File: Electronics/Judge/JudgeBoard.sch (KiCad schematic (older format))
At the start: 21 parts, among them J1 RJ12-UNSHLD, U1 74HC165, U2 74HC165

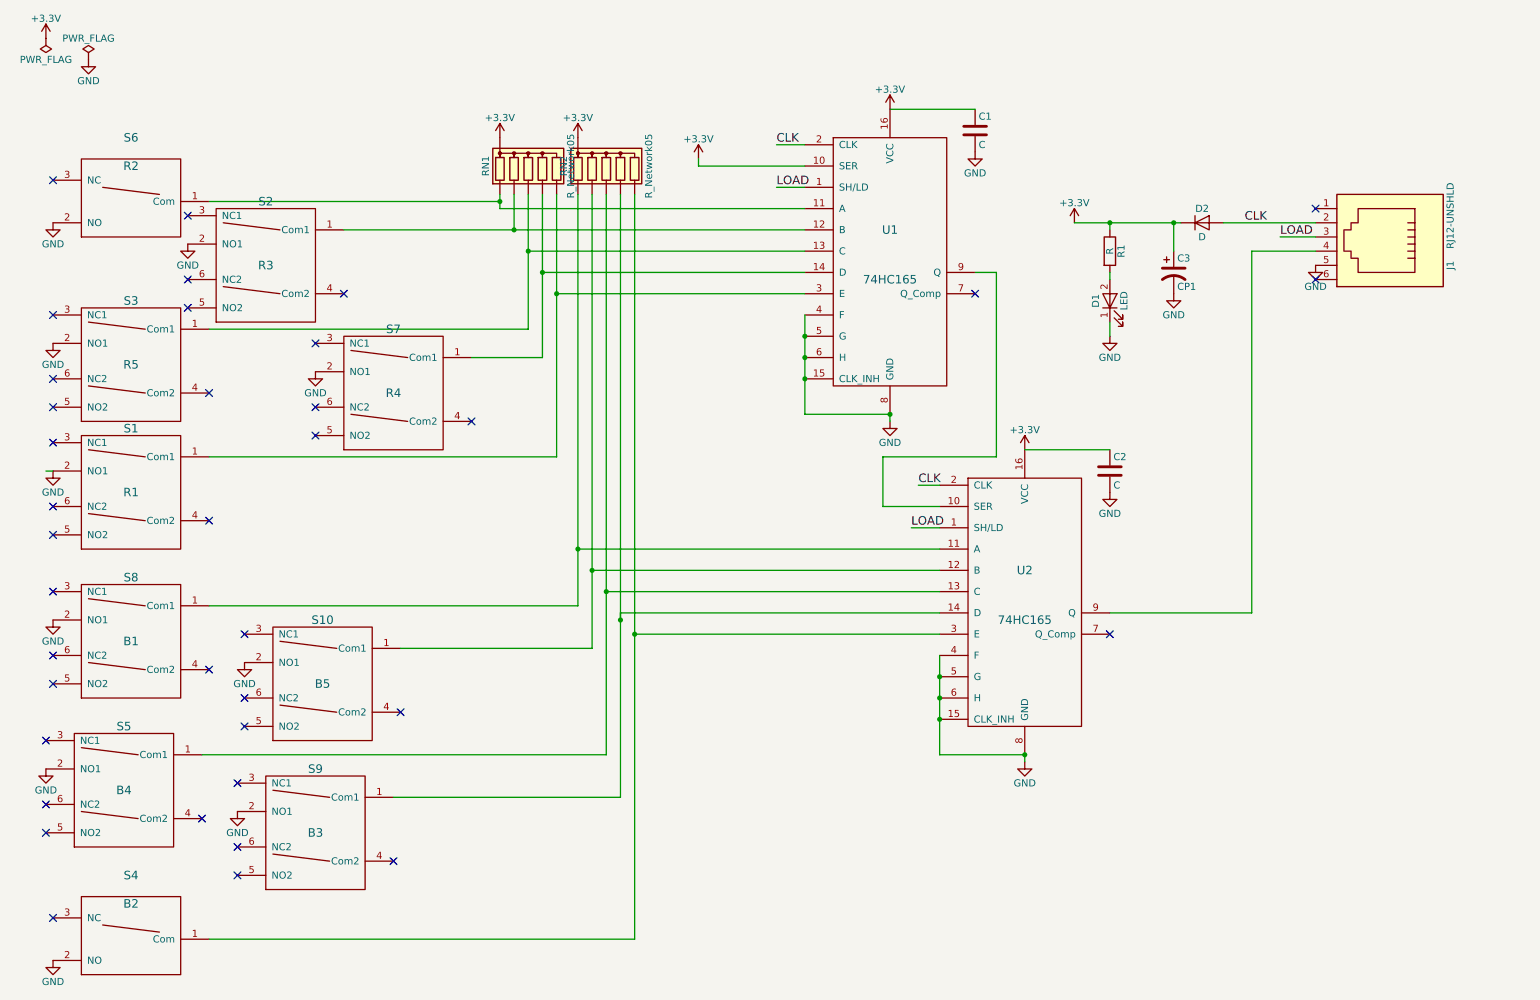
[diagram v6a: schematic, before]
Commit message: Added circuit protection elements to judge controller schematic
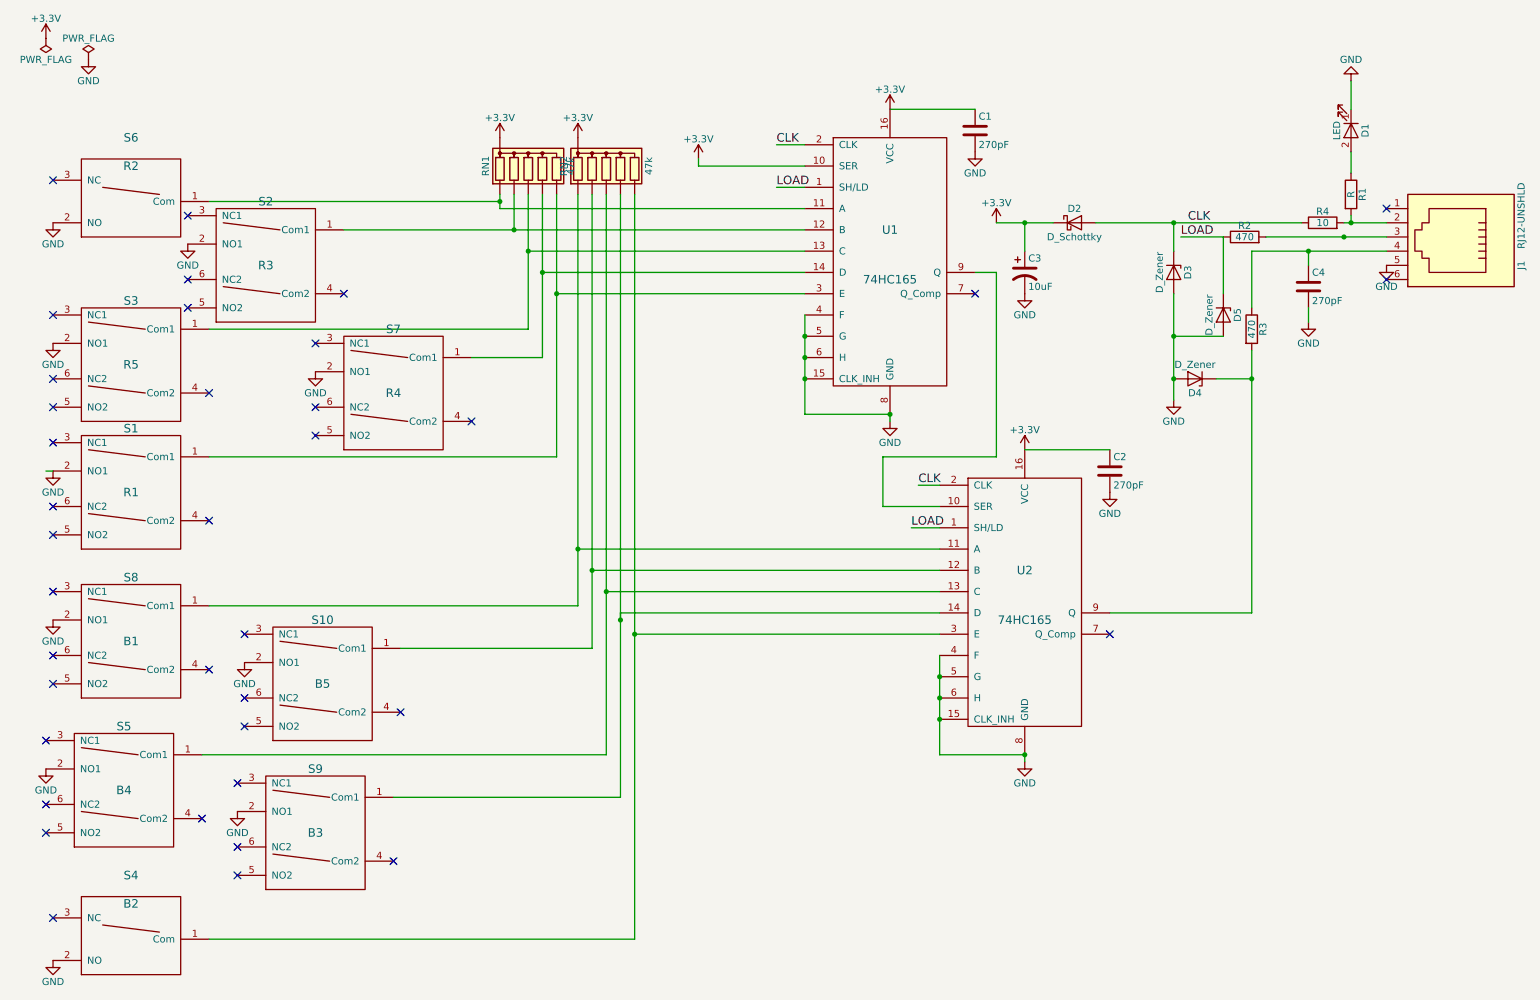
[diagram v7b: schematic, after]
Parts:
- removed D2: D, Diodes_THT:D_DO-35_SOD27_P5.08mm_Vertical_AnodeUp, symbol D
- added C4: 270pF, Capacitors_THT:C_Disc_D3.4mm_W2.1mm_P2.50mm, symbol C
- added D2: D_Schottky, symbol D_Schottky
- added D3, D4, D5: D_Zener, symbol D_Zener
- added R2, R3: 470, Resistors_THT:R_Axial_DIN0207_L6.3mm_D2.5mm_P2.54mm_Vertical, symbol R
- added R4: 10, Resistors_THT:R_Axial_DIN0207_L6.3mm_D2.5mm_P2.54mm_Vertical, symbol R
- C1, C2: value C -> 270pF
- C3: value CP1 -> 10uF
- RN1, RN2: value R_Network05 -> 47k
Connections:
- net +3V3: now also D2.1 (K); no longer R1.1
- net CLK: now also D2.2 (A), D3.1 (K), R4.1; no longer J1.2
- net GND: now also C4.2, D3.2 (A), D4.2 (A), D5.2 (A)
- net LOAD: now also D5.1 (K), R2.1; no longer J1.3
- net at U2.9 (Q): now also D4.1 (K), R3.2; no longer J1.4
- net at R1.2: now also J1.2, R4.2; no longer D1.2 (A)
- new net: J1.3, R2.2
- new net: C4.1, J1.4, R3.1
- new net: D1.2 (A), R1.1
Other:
- moved on the sheet: C3, D1, J1, R1

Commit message: Finalized component selection for Judge Controller
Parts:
- R1: value R -> 68
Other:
- moved on the sheet: D3, D4, D5, R2, R3
